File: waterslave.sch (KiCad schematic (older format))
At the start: 30 parts, among them IC1 ATMEGA328P-P, P1 CONN_3X2, P2 CONN_4, P3 CONN_2, P4 CONN_6, P5 CONN_2, P6 CONN_1, P7 CONN_1, P8 CONN_1, P9 CONN_1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

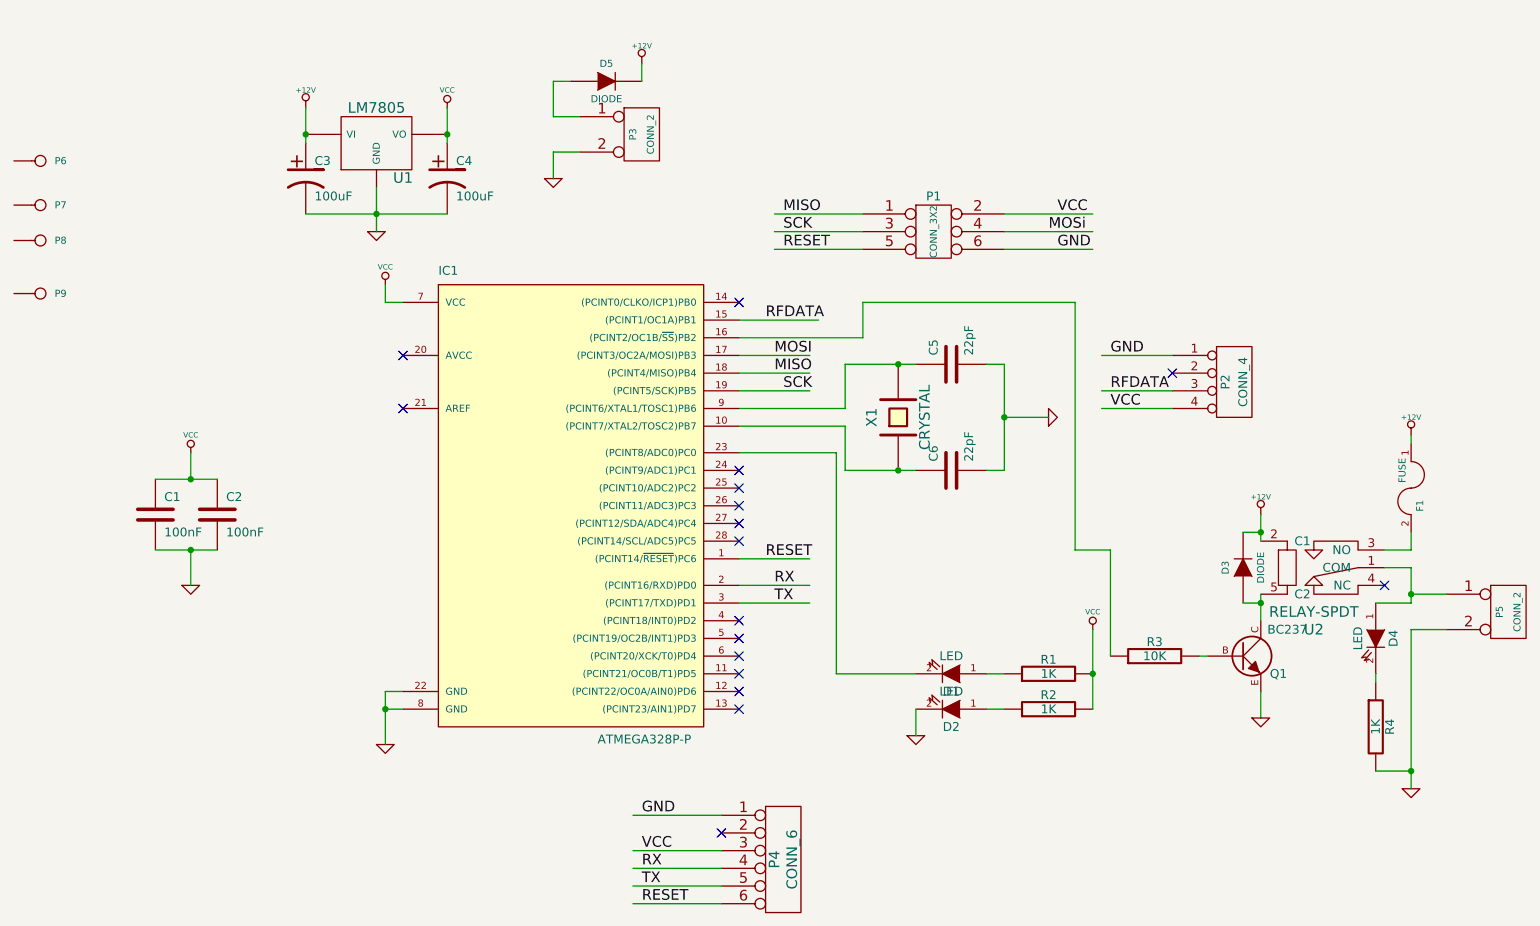
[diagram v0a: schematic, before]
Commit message: Redesign for TQFP-32 version of ATmega328P, move diode
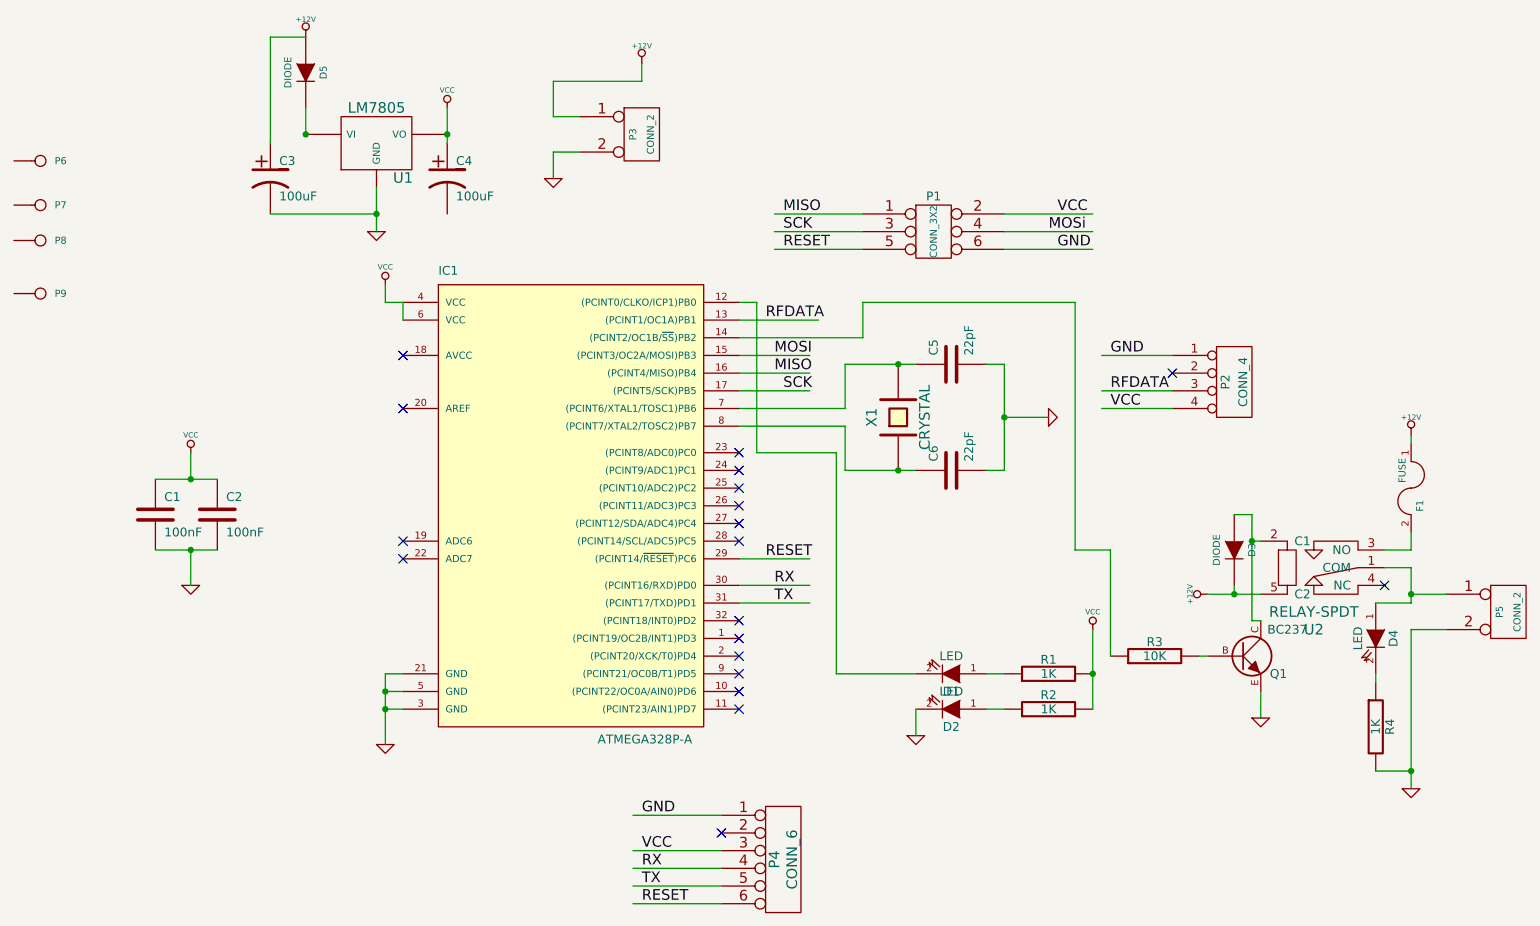
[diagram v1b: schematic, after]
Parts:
- removed IC1: ATMEGA328P-P, DIL28, symbol ATMEGA328P-P
- added IC1: ATMEGA328P-A, TQFP32, symbol ATMEGA328P-A
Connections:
- wire segments 80 -> 88
- no-connect marks 17 -> 19
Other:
- moved on the sheet: C3, D3, D5
